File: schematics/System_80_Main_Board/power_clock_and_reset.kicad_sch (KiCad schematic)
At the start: 34 parts, among them J3 Power, SW1 RESET, U1 74LS14, U101 7805, U102 7812, U14 74LS132, U2 74LS05, U37 74LS367, U38 74LS92, U39 74LS74, U40 74LS74

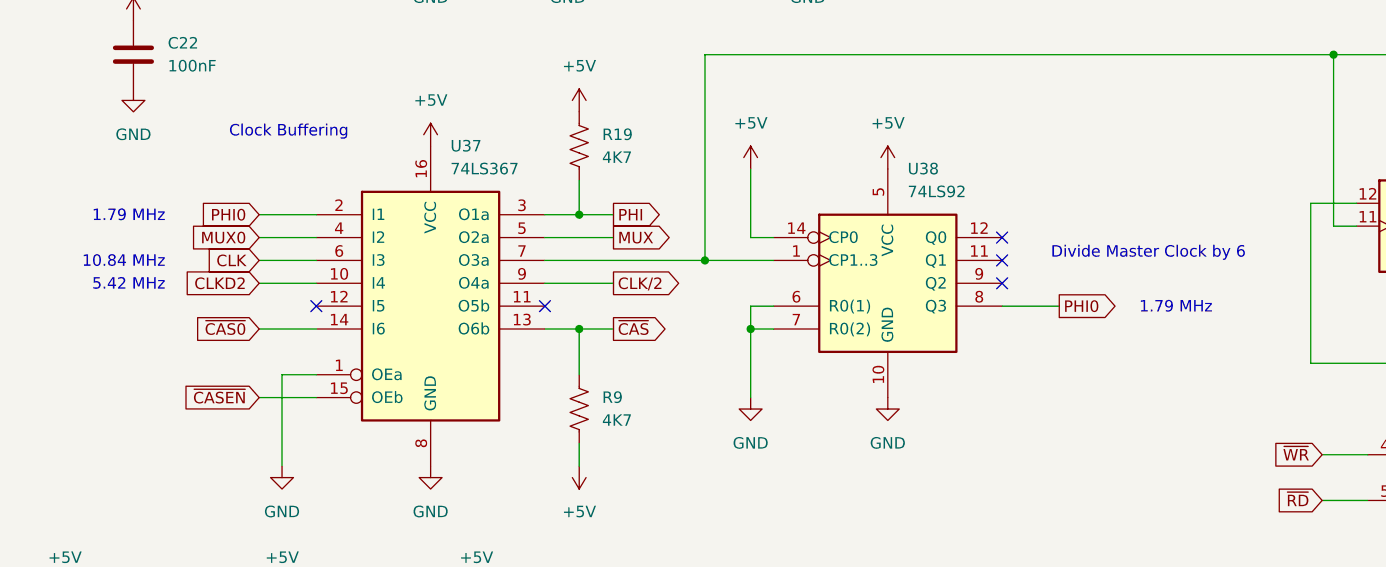
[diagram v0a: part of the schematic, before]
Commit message: Schematic for the System 80 video/cassette board
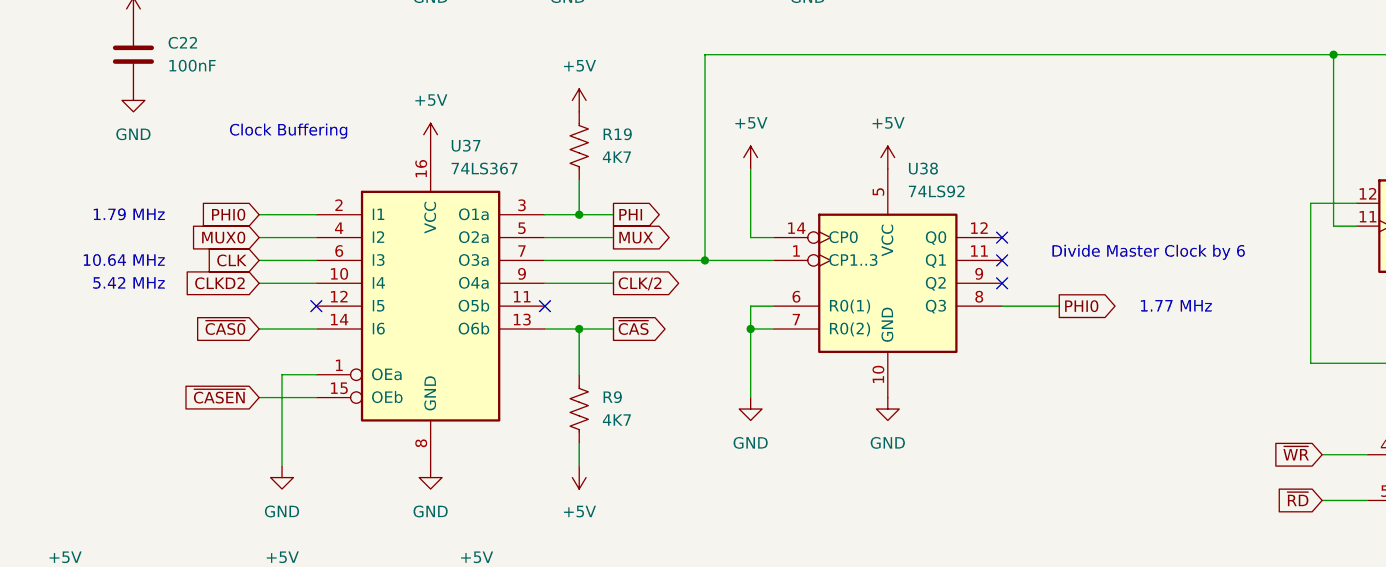
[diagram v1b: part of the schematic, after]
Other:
- note added: "1.77 MHz"
- note added: "10.64 MHz"
- note removed: "10.84 MHz"
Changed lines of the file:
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@@
 		)
 	)
-	(text "10.84 MHz"
+	(text "10.64 MHz"
 		(exclude_from_sim no)
 		(at 37.846 124.714 0)
@@
 		)
 	)
-	(text "1.79 MHz"
+	(text "1.77 MHz"
 		(exclude_from_sim no)
 		(at 150.114 129.794 0)

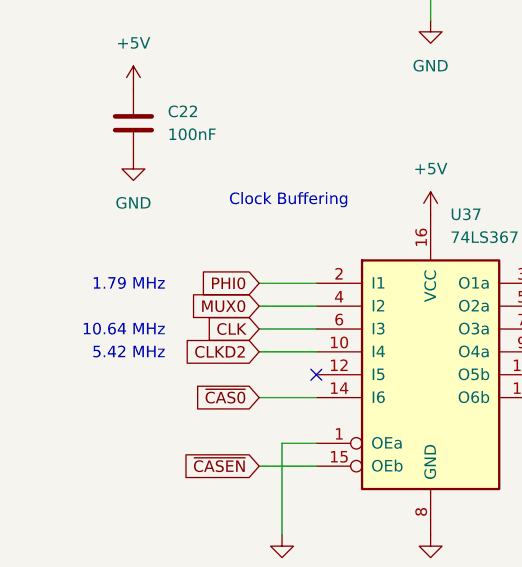
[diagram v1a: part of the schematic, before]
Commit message: Fix the CPU clock frequency: 1.77MHz, not 1.79MHz
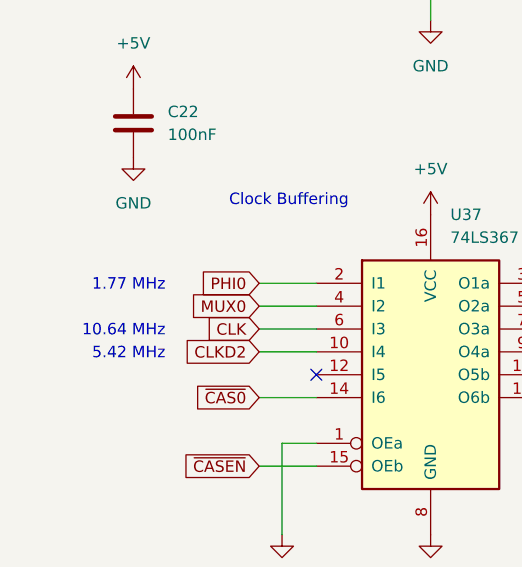
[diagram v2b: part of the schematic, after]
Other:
- note removed: "1.79 MHz"
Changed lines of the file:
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@@
 		)
 	)
-	(text "1.79 MHz"
+	(text "1.77 MHz"
 		(exclude_from_sim no)
 		(at 37.846 119.634 0)
